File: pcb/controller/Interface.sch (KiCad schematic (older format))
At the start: 0 parts

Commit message: controller schematic capture almost done
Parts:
- added J?: RJ45_Shielded, symbol Connector:RJ45_Shielded
- added Q?: Q_NMOS_GSD, symbol Device:Q_NMOS_GSD
- added R?: R, symbol Device:R
- added U?: ISO3086DWR, symbol wbraun_ic_lib:ISO3086DWR
- added U? (x3): RFM-0505S, symbol wbraun_ic_lib:RFM-0505S
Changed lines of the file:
@@
 $Descr A4 11693 8268
 encoding utf-8
-Sheet 1 6
+Sheet 6 7
 Title ""
 Date ""
@@
 Comment4 ""
 $EndDescr
+$Comp
+L wbraun_ic_lib:ISO3086DWR U?
+U 1 1 5C705166
+P 3000 2550
+F 0 "U?" H 3000 3265 50  0000 C CNN
+F 1 "ISO3086DWR" H 3000 3174 50  0000 C CNN
+F 2 "" H 2450 3050 50  0001 C CNN
+F 3 "" H 2450 3050 50  0001 C CNN
+	1    3000 2550
+	1    0    0    -1
+$EndComp
+$Comp
+L wbraun_ic_lib:RFM-0505S U?
+U 1 1 5C705DF8
+P 2950 1250
+F 0 "U?" H 2950 1637 60  0000 C CNN
+F 1 "RFM-0505S" H 2950 1531 60  0000 C CNN
+F 2 "" H 2950 1250 60  0001 C CNN
+F 3 "" H 2950 1250 60  0001 C CNN
+	1    2950 1250
+	1    0    0    -1
+$EndComp
+$Comp
+L wbraun_ic_lib:RFM-0505S U?
+U 1 1 5C705F02
+P 4150 6900
+F 0 "U?" H 4150 7287 60  0000 C CNN
+F 1 "RFM-0505S" H 4150 7181 60  0000 C CNN
+F 2 "" H 4150 6900 60  0001 C CNN
+F 3 "" H 4150 6900 60  0001 C CNN
+	1    4150 6900
+	1    0    0    -1
+$EndComp
+$Comp
+L wbraun_ic_lib:RFM-0505S U?
+U 1 1 5C705FD9
+P 2500 4800
+F 0 "U?" H 2500 5187 60  0000 C CNN
+F 1 "RFM-0505S" H 2500 5081 60  0000 C CNN
+F 2 "" H 2500 4800 60  0001 C CNN
+F 3 "" H 2500 4800 60  0001 C CNN
+	1    2500 4800
+	1    0    0    -1
+$EndComp
+$Comp
+L Device:Q_NMOS_GSD Q?
+U 1 1 5C7061B0
+P 1750 5250
+F 0 "Q?" H 1955 5296 50  0000 L CNN
+F 1 "Q_NMOS_GSD" H 1955 5205 50  0000 L CNN
+F 2 "" H 1950 5350 50  0001 C CNN
+F 3 "~" H 1750 5250 50  0001 C CNN
+	1    1750 5250
+	1    0    0    -1
+$EndComp
+$Comp
+L Device:R R?
+U 1 1 5C7063E5
+P 1350 5500
+F 0 "R?" H 1420 5546 50  0000 L CNN
+F 1 "R" H 1420 5455 50  0000 L CNN
+F 2 "" V 1280 5500 50  0001 C CNN
+F 3 "~" H 1350 5500 50  0001 C CNN
+	1    1350 5500
+	1    0    0    -1
+$EndComp
+$Comp
+L Connector:RJ45_Shielded J?
+U 1 1 5C7071D7
+P 5250 2550
+F 0 "J?" H 4921 2591 50  0000 R CNN
+F 1 "RJ45_Shielded" H 4921 2500 50  0000 R CNN
+F 2 "" V 5250 2575 50  0001 C CNN
+F 3 "~" V 5250 2575 50  0001 C CNN
+	1    5250 2550
+	-1   0    0    -1
+$EndComp
 $EndSCHEMATC

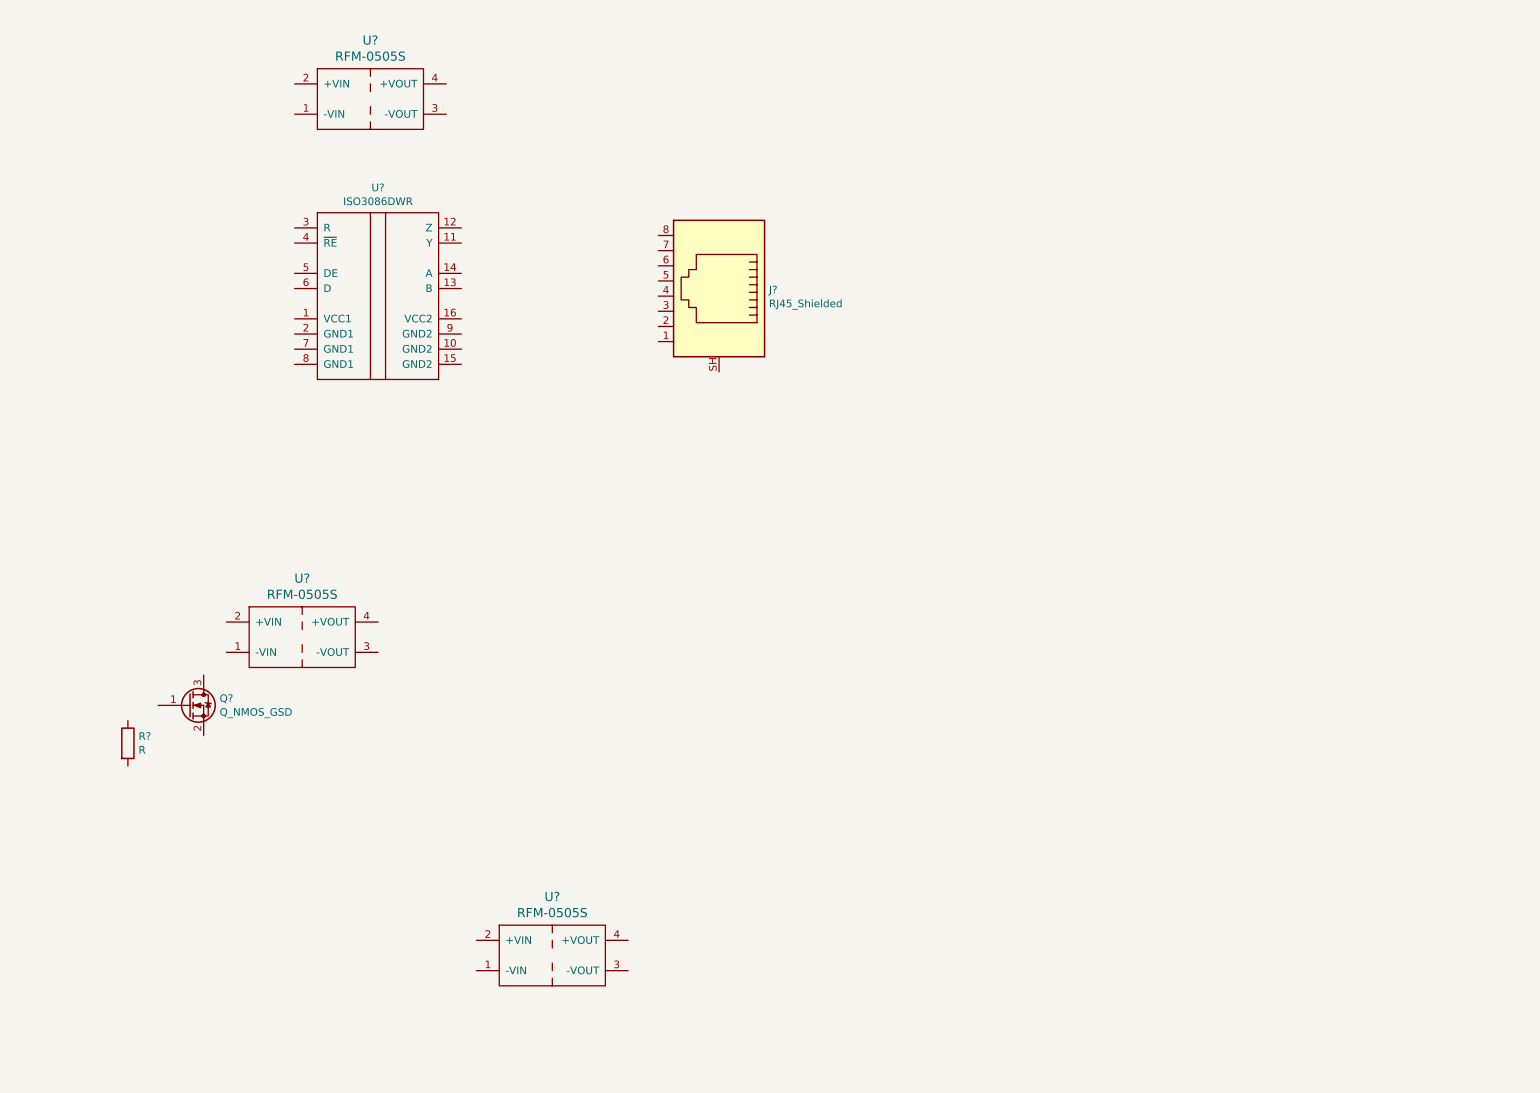
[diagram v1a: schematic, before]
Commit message: started assigning footprints
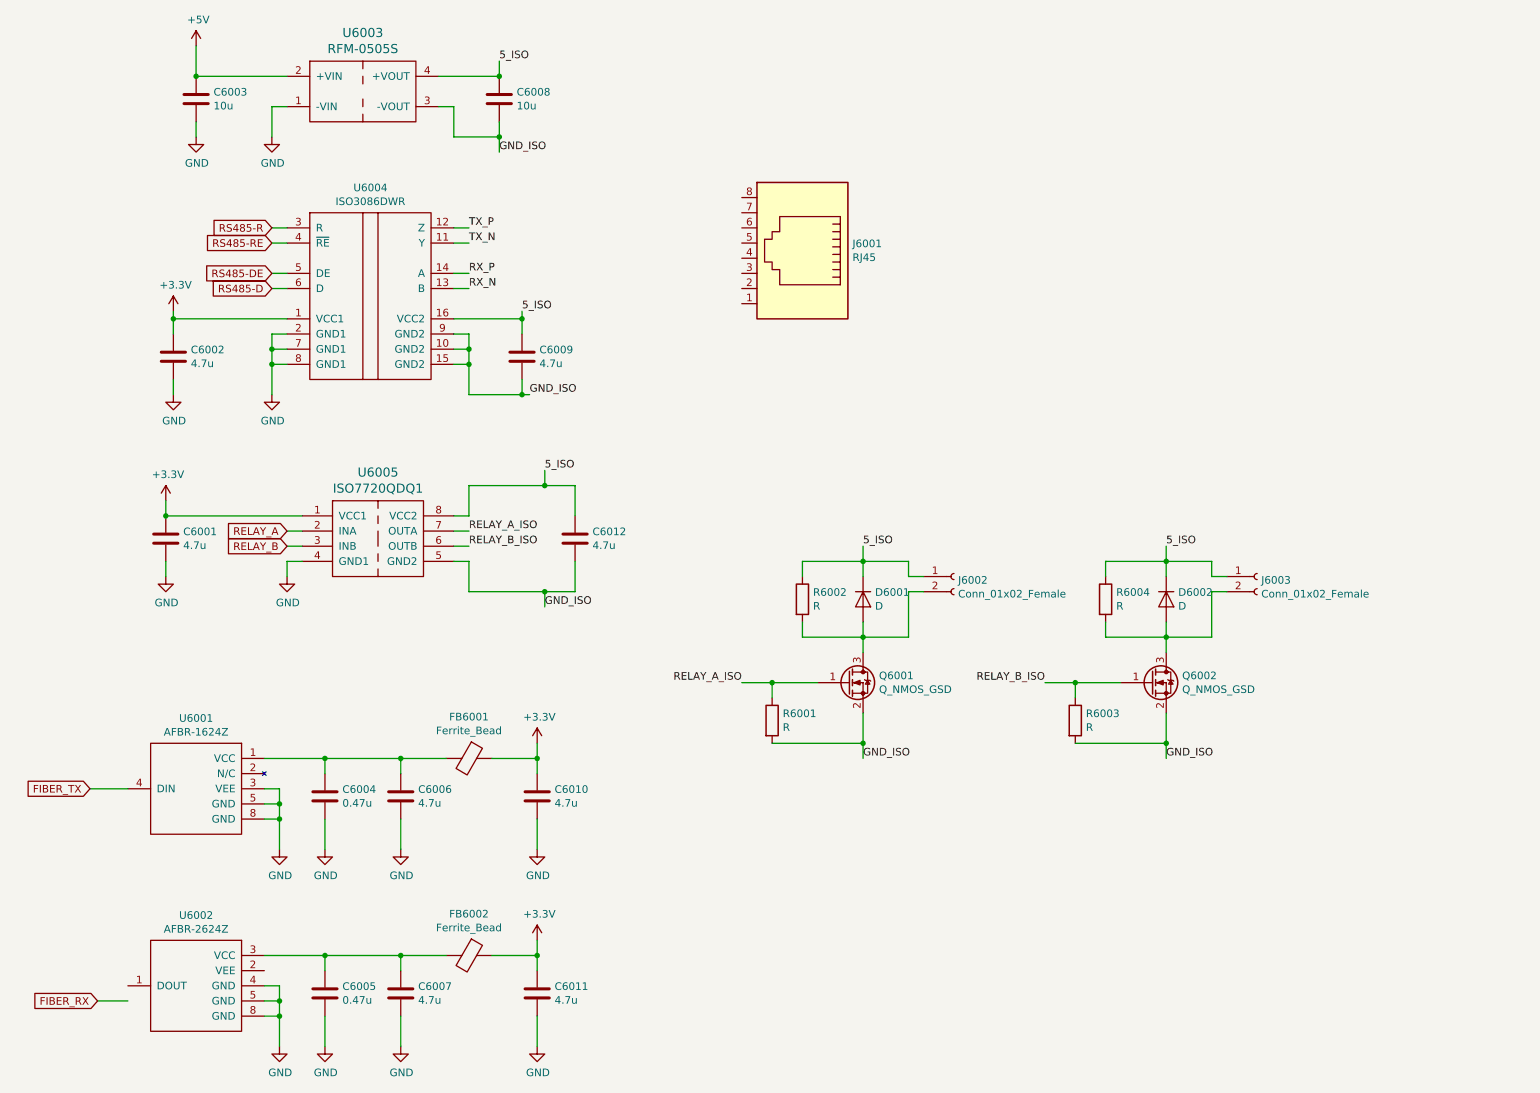
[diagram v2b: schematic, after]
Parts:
- removed J?: RJ45_Shielded, symbol Connector:RJ45_Shielded
- removed R?: R, symbol Device:R
- removed U? (x2): RFM-0505S, symbol wbraun_ic_lib:RFM-0505S
- added C6001, C6002, C6006, C6007, C6009, C6010, C6011, C6012: 4.7u, symbol Device:C
- added C6003, C6008: 10u, symbol Device:C
- added C6004, C6005: 0.47u, symbol Device:C
- added D6001, D6002: D, symbol Device:D
- added FB6001, FB6002: Ferrite_Bead, symbol Device:Ferrite_Bead
- added J6001: RJ45, symbol Connector:RJ45
- added J6002, J6003: Conn_01x02_Female, symbol Connector:Conn_01x02_Female
- added Q6002: Q_NMOS_GSD, symbol Device:Q_NMOS_GSD
- added R6001, R6002, R6003, R6004: R, symbol Device:R
- added U6001: AFBR-1624Z, symbol wbraun_ic_lib:AFBR-1624Z
- added U6002: AFBR-2624Z, symbol wbraun_ic_lib:AFBR-2624Z
- added U6005: ISO7720QDQ1, symbol wbraun_ic_lib:ISO7720QDQ1
- gave numbers to parts that had none: 3
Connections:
- net +3V3: now reaches U6004.1 (VCC1)
- net +3V3: now also C6001.1, C6002.1, C6010.1, C6011.1, FB6001.1, FB6002.1, U6005.1 (VCC1)
- net GND_ISO: now reaches U6004.10 (GND2)
- net GND_ISO: now also Q6001.2 (S), U6003.3 (-VOUT), U6004.15 (GND2), U6004.9 (GND2), C6008.2, C6009.2, C6012.2, Q6002.2 (S), R6001.2, R6003.2, U6005.5 (GND2)
- net TX_N: now reaches U6004.11 (Y)
- net TX_P: now reaches U6004.12 (Z)
- net RX_N: now reaches U6004.13 (B)
- net RX_P: now reaches U6004.14 (A)
- net 5_ISO: now reaches U6004.16 (VCC2)
- net 5_ISO: now also U6003.4 (+VOUT), C6008.1, C6009.1, C6012.1, D6001.1 (K), D6002.1 (K), J6002.1 (Pin_1), J6003.1 (Pin_1), R6002.1, R6004.1, U6005.8 (VCC2)
- net GND: now reaches U6004.2 (GND1)
- net GND: now also U6003.1 (-VIN), U6004.7 (GND1), U6004.8 (GND1), C6001.2, C6002.2, C6003.2, C6004.2, C6005.2, C6006.2, C6007.2, C6010.2, C6011.2, U6001.3 (VEE), U6001.5 (GND), U6001.8 (GND), U6002.4 (GND), U6002.5 (GND), U6002.8 (GND), U6005.4 (GND1)
- net RS485-R: now reaches U6004.3 (R)
- net RS485-RE: now reaches U6004.4 (~RE)
- net RS485-DE: now reaches U6004.5 (DE)
- net RS485-D: now reaches U6004.6 (D)
- net +5V: now reaches U6003.2 (+VIN)
- net +5V: now also C6003.1
- net RELAY_A_ISO: now reaches Q6001.1 (G)
- net RELAY_A_ISO: now also R6001.1, U6005.7 (OUTA)
- net at Q6001.3 (D): now also D6001.2 (A), J6002.2 (Pin_2), R6002.2
- new net: D6002.2 (A), J6003.2 (Pin_2), Q6002.3 (D), R6004.2
- new net: C6004.1, C6006.1, FB6001.2, U6001.1 (VCC)
- new net: C6005.1, C6007.1, FB6002.2, U6002.3 (VCC)
- new net FIBER_TX: U6001.4 (DIN)
- new net RELAY_A: U6005.2 (INA)
- new net RELAY_B: U6005.3 (INB)
- new net RELAY_B_ISO: Q6002.1 (G), R6003.1, U6005.6 (OUTB)
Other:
- moved on the sheet: Q6001, U6003, U6004

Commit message: pcb component placement almost done
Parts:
- removed D6001, D6002: D, symbol Device:D
- removed Q6001, Q6002: Q_NMOS_GSD, symbol Device:Q_NMOS_GSD
- removed R6003, R6004: R, symbol Device:R
- added U6006: ULN2003F12, Package_DFN_QFN:DFN-10-1EP_3x3mm_P0.5mm_EP1.55x2.48mm, symbol wbraun_ic_lib:ULN2003F12
- C6001, C6002, C6004, C6005, C6006, C6007, C6009, C6010, C6011, C6012: footprint (none) -> Capacitor_SMD:C_0402_1005Metric
- C6003: footprint (none) -> Capacitor_SMD:C_0805_2012Metric
- C6008: value 10u -> 47u; footprint (none) -> Capacitor_SMD:C_0805_2012Metric
- FB6001, FB6002: footprint (none) -> Inductor_SMD:L_0805_2012Metric
- J6001: footprint (none) -> Connector_RJ:RJ45_Amphenol_54602-x08_Horizontal
- J6002, J6003: footprint (none) -> wbraun_smd:terminalBlock-3.5mm-2
- R6001, R6002: footprint (none) -> Resistor_SMD:R_0402_1005Metric
- U6001, U6002: footprint (none) -> wbraun_smd:versatile-link_horizontal
- U6003: footprint (none) -> wbraun_smd:RFM-0505S
- U6004: footprint (none) -> Package_SO:SOIC-16W_7.5x10.3mm_P1.27mm
- U6005: footprint (none) -> Package_SO:SOIC-8_3.9x4.9mm_P1.27mm
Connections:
- net 5_ISO: now also U6006.6 (COM); no longer R6002.1
- net FIBER_RX: now also U6002.1 (DOUT)
- net GND: now also R6001.2, R6002.2, U6002.2 (VEE)
- net GND_ISO: now also U6006.11 (EP), U6006.5 (GND); no longer R6001.2
- net RELAY_A: now also R6001.1
- net RELAY_A_ISO: now also U6006.1 (IN1); no longer R6001.1
- net RELAY_B: now also R6002.1
- net RELAY_B_ISO: now also U6006.2 (IN2)
- net RELAY_B_DRV: now reaches J6002.2 (Pin_2)
- net RELAY_B_DRV: now also U6006.8 (OUT3); no longer R6002.2
- net RELAY_A_DRV: now reaches J6003.2 (Pin_2)
- net RELAY_A_DRV: now also U6006.7 (OUT4)
- net +3V3 renamed +3V3D
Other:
- moved on the sheet: J6002, J6003

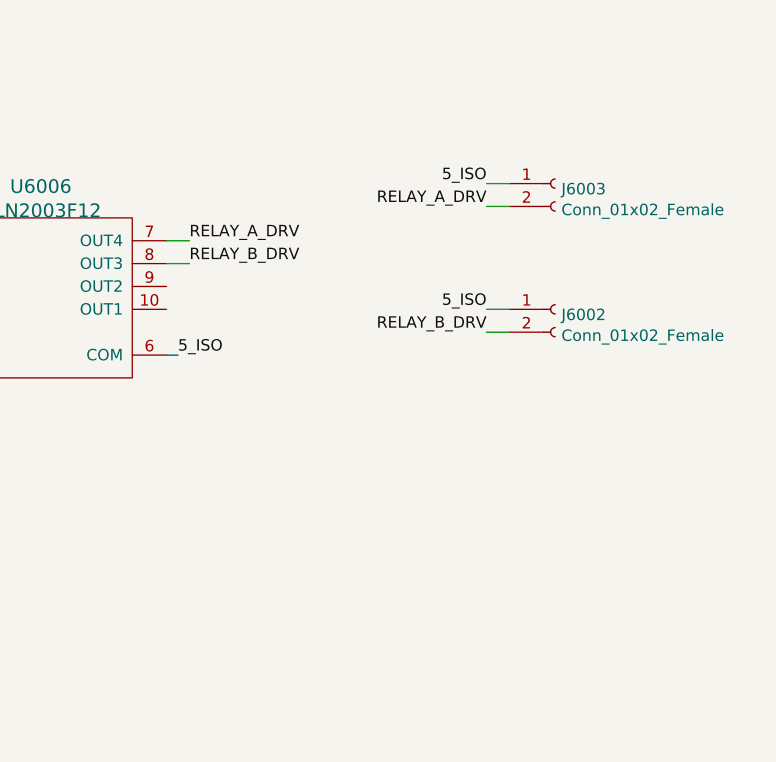
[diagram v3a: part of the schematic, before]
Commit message: controller PCB routing progress
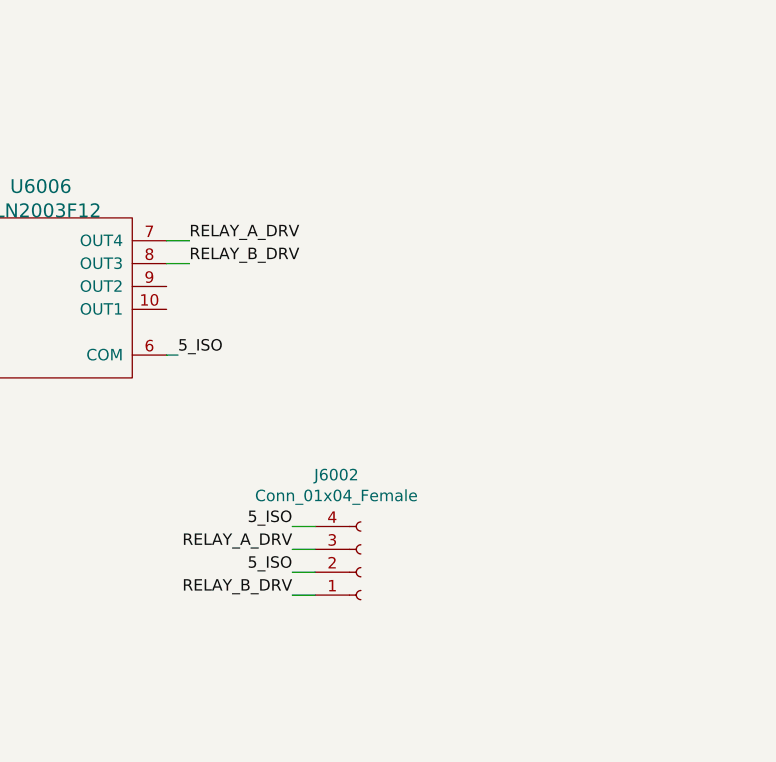
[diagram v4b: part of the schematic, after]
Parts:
- removed J6002, J6003: Conn_01x02_Female, wbraun_smd:terminalBlock-3.5mm-2, symbol Connector:Conn_01x02_Female
- added J6002: Conn_01x04_Female, wbraun_smd:Terminal-block-plug_4x1_3.5mm-pitch, symbol Connector:Conn_01x04_Female
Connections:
- net 5_ISO: now also J6002.2 (Pin_2), J6002.4 (Pin_4)
- net RELAY_A_DRV: now also J6002.3 (Pin_3)
- net RELAY_B_DRV: now also J6002.1 (Pin_1)
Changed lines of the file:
@@
-$EndComp
-$Comp
-L Connector:Conn_01x02_Female J6002
-U 1 1 5C429B27
-P 9700 3700
-F 0 "J6002" H 9727 3676 50  0000 L CNN
-F 1 "Conn_01x02_Female" H 9727 3585 50  0000 L CNN
-F 2 "wbraun_smd:terminalBlock-3.5mm-2" H 9700 3700 50  0001 C CNN
-F 3 "~" H 9700 3700 50  0001 C CNN
-	1    9700 3700
-	1    0    0    -1
 $EndComp
 $Comp
@@
 Text Label 6700 3800 2    50   ~ 0
 GND_ISO
-Text Label 9400 3150 2    50   ~ 0
+Text Label 8550 4650 2    50   ~ 0
 5_ISO
-$Comp
-L Connector:Conn_01x02_Female J6003
-U 1 1 5C42EA70
-P 9700 3150
-F 0 "J6003" H 9727 3126 50  0000 L CNN
-F 1 "Conn_01x02_Female" H 9727 3035 50  0000 L CNN
-F 2 "wbraun_smd:terminalBlock-3.5mm-2" H 9700 3150 50  0001 C CNN
-F 3 "~" H 9700 3150 50  0001 C CNN
-	1    9700 3150
-	1    0    0    -1
-$EndComp
 Text Label 8050 3900 0    50   ~ 0
 5_ISO
@@
 Text Label 8100 3500 0    50   ~ 0
 RELAY_B_DRV
-Text Label 9400 3700 2    50   ~ 0
+Text Label 8550 4850 2    50   ~ 0
 5_ISO
-Text Label 9400 3250 2    50   ~ 0
+Text Label 8550 4750 2    50   ~ 0
 RELAY_A_DRV
-Text Label 9400 3800 2    50   ~ 0
+Text Label 8550 4950 2    50   ~ 0
 RELAY_B_DRV
 Wire Wire Line
-	9400 3150 9500 3150
-Wire Wire Line
-	9400 3250 9500 3250
-Wire Wire Line
-	9400 3700 9500 3700
-Wire Wire Line
-	9400 3800 9500 3800
+	8550 4650 8650 4650
+Wire Wire Line
+	8550 4750 8650 4750
+Wire Wire Line
+	8550 4850 8650 4850
+Wire Wire Line
+	8550 4950 8650 4950
 Wire Wire Line
 	6900 3900 6800 3900
@@
 Text GLabel 6200 5400 1    50   Input ~ 0
 RELAY_B
+$Comp
+L Connector:Conn_01x04_Female J6002
+U 1 1 5C461B4F
+P 8850 4850
+F 0 "J6002" H 8743 4425 50  0000 C CNN
+F 1 "Conn_01x04_Female" H 8743 4516 50  0000 C CNN
+F 2 "wbraun_smd:Terminal-block-plug_4x1_3.5mm-pitch" H 8850 4850 50  0001 C CNN
+F 3 "~" H 8850 4850 50  0001 C CNN
+	1    8850 4850
+	1    0    0    1
+$EndComp
 $EndSCHEMATC

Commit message: routing almost done
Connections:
- net 5_ISO: now also J6001.7
- net GND_ISO: now also J6001.8
- net RX_N: now also J6001.6
- net RX_P: now also J6001.3
- net TX_N: now also J6001.2
- net TX_P: now also J6001.1
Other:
- note added: "Connect with RJ45 Crossover Cable\n(1 Swapped with 3, 2 Swapped with 6)"
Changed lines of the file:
@@
 	1    0    0    1
 $EndComp
+Text Notes 5300 1150 0    50   ~ 0
+Connect with RJ45 Crossover Cable\n(1 Swapped with 3, 2 Swapped with 6)
+Wire Wire Line
+	5400 2600 5300 2600
+Wire Wire Line
+	5400 2500 5300 2500
+Wire Wire Line
+	5400 2400 5300 2400
+Wire Wire Line
+	5400 2100 5300 2100
+Text Label 5300 2600 2    50   ~ 0
+TX_P
+Text Label 5300 2500 2    50   ~ 0
+TX_N
+Text Label 5300 2400 2    50   ~ 0
+RX_P
+Text Label 5300 2100 2    50   ~ 0
+RX_N
+Wire Wire Line
+	5400 2000 5300 2000
+Wire Wire Line
+	5400 1900 5300 1900
+Text Label 5300 1900 2    50   ~ 0
+GND_ISO
+Text Label 5300 2000 2    50   ~ 0
+5_ISO
 $EndSCHEMATC

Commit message: controller layout done and schematic reviewed
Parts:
- added R6003: 120, Resistor_SMD:R_1206_3216Metric, symbol Device:R
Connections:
- net RX_N: now also R6003.2
- net RX_P: now also R6003.1
- net TX_N: now also U6004.12 (Z); no longer U6004.11 (Y)
- net TX_P: now also U6004.11 (Y); no longer U6004.12 (Z)
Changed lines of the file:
@@
 Wire Wire Line
 	3500 2500 3600 2500
+Text Label 3600 2200 0    50   ~ 0
+TX_P
 Text Label 3600 2100 0    50   ~ 0
-TX_P
-Text Label 3600 2200 0    50   ~ 0
 TX_N
 Text Label 3600 2400 0    50   ~ 0
@@
 Text Label 5300 2000 2    50   ~ 0
 5_ISO
+$Comp
+L Device:R R6003
+U 1 1 5C498237
+P 6800 2250
+F 0 "R6003" H 6870 2296 50  0000 L CNN
+F 1 "120" H 6870 2205 50  0000 L CNN
+F 2 "Resistor_SMD:R_1206_3216Metric" V 6730 2250 50  0001 C CNN
+F 3 "~" H 6800 2250 50  0001 C CNN
+	1    6800 2250
+	1    0    0    -1
+$EndComp
+Wire Wire Line
+	6800 2100 6800 2000
+Wire Wire Line
+	6800 2400 6800 2500
+Text Label 6800 2000 2    50   ~ 0
+RX_P
+Text Label 6800 2500 2    50   ~ 0
+RX_N
 $EndSCHEMATC

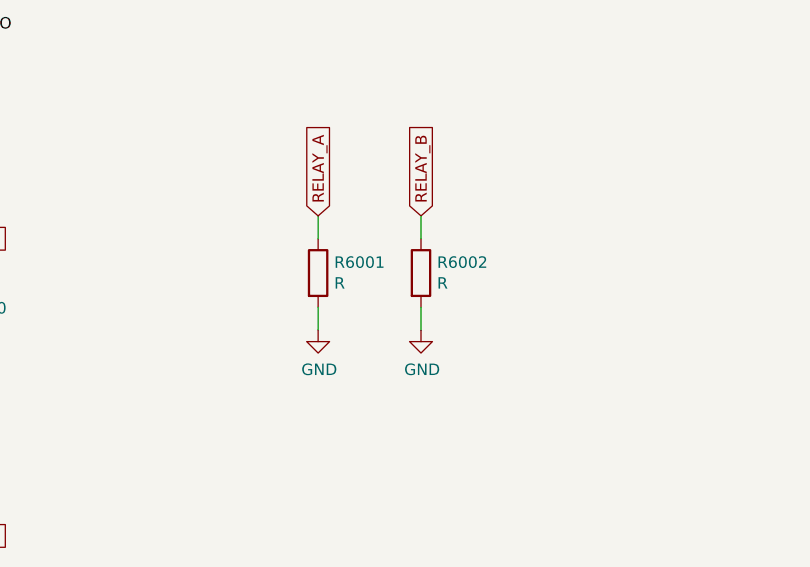
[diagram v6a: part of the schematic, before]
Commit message: updated schematic component values
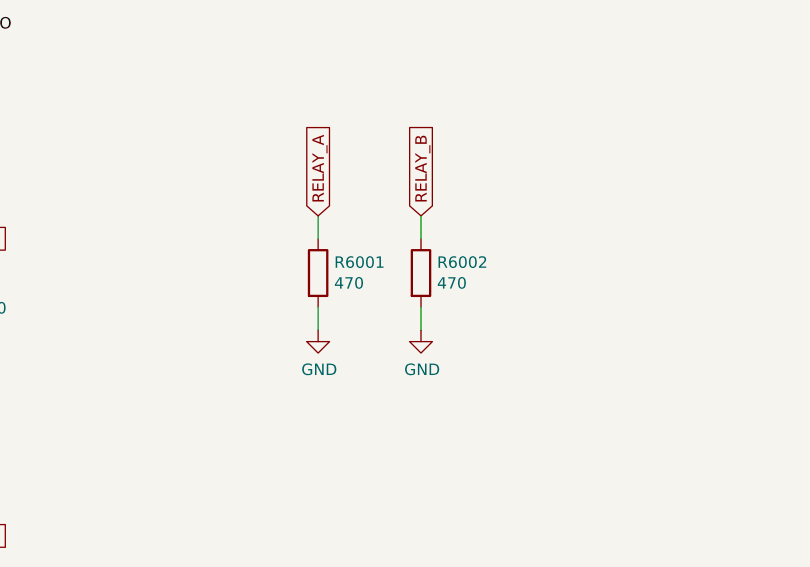
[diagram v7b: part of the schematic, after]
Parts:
- R6001, R6002: value R -> 470
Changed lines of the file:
@@
 P 5750 5650
 F 0 "R6001" H 5820 5696 50  0000 L CNN
-F 1 "R" H 5820 5605 50  0000 L CNN
+F 1 "470" H 5820 5605 50  0000 L CNN
 F 2 "Resistor_SMD:R_0402_1005Metric" V 5680 5650 50  0001 C CNN
 F 3 "~" H 5750 5650 50  0001 C CNN
@@
 P 6200 5650
 F 0 "R6002" H 6270 5696 50  0000 L CNN
-F 1 "R" H 6270 5605 50  0000 L CNN
+F 1 "470" H 6270 5605 50  0000 L CNN
 F 2 "Resistor_SMD:R_0402_1005Metric" V 6130 5650 50  0001 C CNN
 F 3 "~" H 6200 5650 50  0001 C CNN
